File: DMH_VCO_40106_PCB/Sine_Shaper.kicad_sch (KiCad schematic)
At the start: 13 parts, among them Q5 BC548, Q6 BC548, U3 TL074

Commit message: Component placement ongoing
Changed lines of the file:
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@@
+		)
+	)
+	(text_box "Moved R44=1k to Inputs and Outputs sheet"
+		(exclude_from_sim no)
+		(at 179.07 67.31 0)
+		(size 17.78 7.62)
+		(stroke
+			(width 0)
+			(type default)
+		)
+		(fill
+			(type none)
+		)
+		(effects
+			(font
+				(size 1.27 1.27)
+			)
+			(justify left)
 		)
 	)

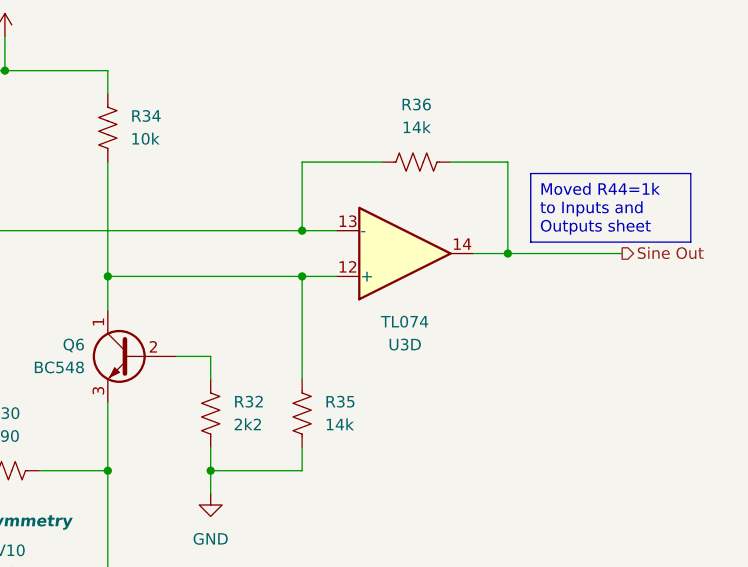
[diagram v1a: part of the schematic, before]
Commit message: Organized Square and Sine Shaper components
Also re-annotated the TL074 ICs to improve the layout
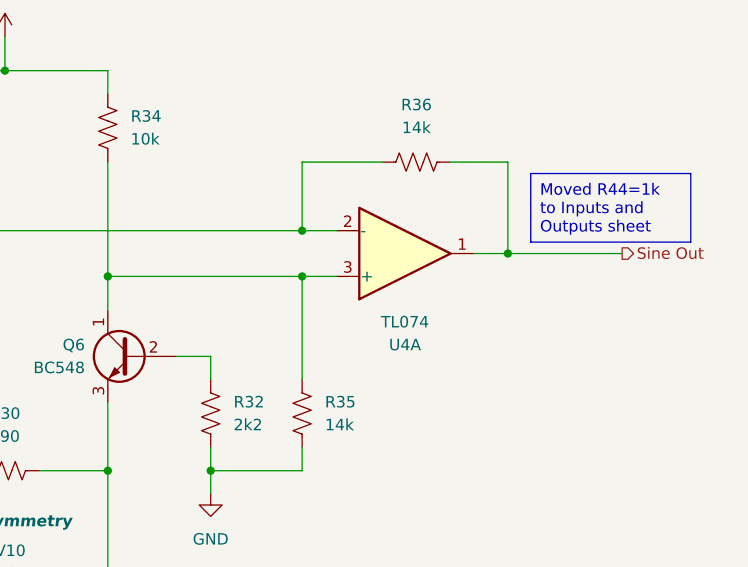
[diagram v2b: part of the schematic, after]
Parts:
- renumbered U3 to U4
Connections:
- net Sine Out: now also U4.1; no longer U4.14
- net at Q5.1 (C), R33.2, R36.1: now also U4.2 (-); no longer U4.13 (-)
- net at Q6.1 (C), R34.2, R35.1: now also U4.3 (+); no longer U4.12 (+)
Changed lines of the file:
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@@
 		(at 165.1 76.2 0)
 		(mirror x)
-		(unit 4)
+		(unit 1)
 		(exclude_from_sim no)
 		(in_bom yes)
 		(on_board yes)
 		(dnp no)
-		(property "Reference" "U3"
+		(property "Reference" "U4"
 			(at 165.1 86.36 0)
 			(effects
@@
 			)
 		)
+		(property "Function" ""
+			(at 165.1 76.2 0)
+			(effects
+				(font
+					(size 1.27 1.27)
+				)
+				(hide yes)
+			)
+		)
 		(pin "9"
 		)
@@
 			(project ""
 				(path "/fefed352-c100-4617-bbfb-c55e7427b122/5d4fa276-24f5-484f-b50d-2ebe5f0666ef"
-					(reference "U3")
-					(unit 4)
+					(reference "U4")
+					(unit 1)
 				)
 			)

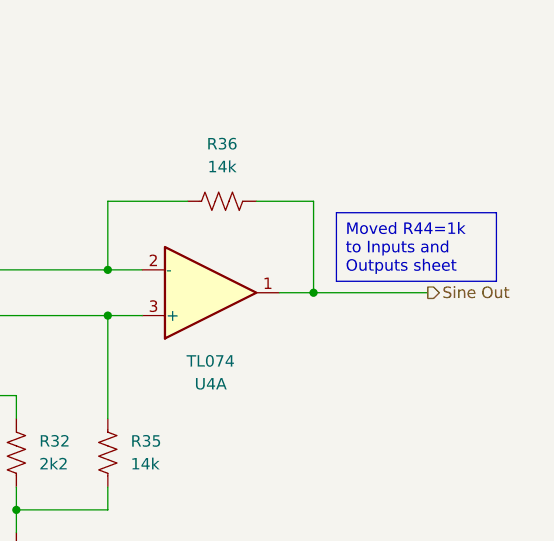
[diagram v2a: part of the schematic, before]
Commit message: Placed input and output resistors back in main PCB
This ensures a more clear schematic and leaves the Connectors PCB only with actual connectors.
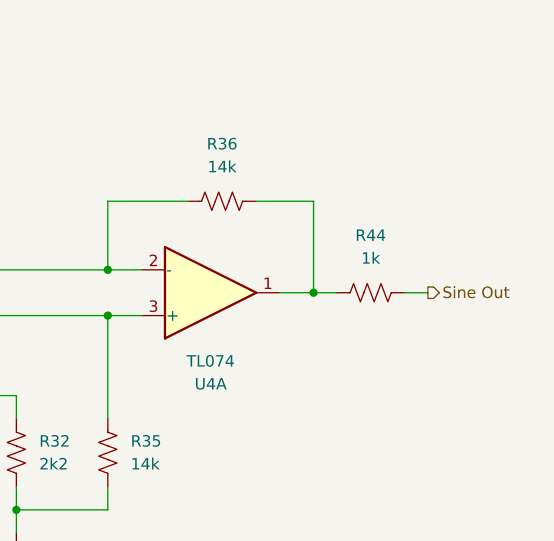
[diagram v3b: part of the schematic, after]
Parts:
- added R44: 1k, Resistor_THT:R_Axial_DIN0207_L6.3mm_D2.5mm_P7.62mm_Horizontal, symbol Device:R_US
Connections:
- net Sine Out: now also R44.1; no longer R36.2, U4.1
- new net: R36.2, R44.2, U4.1
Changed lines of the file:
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@@
 	(wire
 		(pts
-			(xy 176.53 76.2) (xy 189.23 76.2)
+			(xy 176.53 76.2) (xy 179.07 76.2)
 		)
 		(stroke
@@
 	(wire
 		(pts
+			(xy 186.69 76.2) (xy 189.23 76.2)
+		)
+		(stroke
+			(width 0)
+			(type default)
+		)
+	)
+	(wire
+		(pts
 			(xy 132.08 58.42) (xy 132.08 55.88)
 		)
@@
 			(width 0)
 			(type default)
-		)
-	)
-	(text_box "Moved R44=1k to Inputs and Outputs sheet"
-		(exclude_from_sim no)
-		(at 179.07 67.31 0)
-		(size 17.78 7.62)
-		(stroke
-			(width 0)
-			(type default)
-		)
-		(fill
-			(type none)
-		)
-		(effects
-			(font
-				(size 1.27 1.27)
-			)
-			(justify left)
 		)
 	)
@@
 					(unit 1)
 				)
+			)
+		)
+	)
+	(symbol
+		(lib_id "Device:R_US")
+		(at 182.88 76.2 270)
+		(unit 1)
+		(exclude_from_sim no)
+		(in_bom yes)
+		(on_board yes)
+		(dnp no)
+		(fields_autoplaced yes)
+		(property "Reference" "R44"
+			(at 182.88 69.85 90)
+			(effects
+				(font
+					(size 1.27 1.27)
+				)
+			)
+		)
+		(property "Value" "1k"
+			(at 182.88 72.39 90)
+			(effects
+				(font
+					(size 1.27 1.27)
+				)
+			)
+		)
+		(property "Footprint" "Resistor_THT:R_Axial_DIN0207_L6.3mm_D2.5mm_P7.62mm_Horizontal"
+			(at 182.626 77.216 90)
+			(effects
+				(font
+					(size 1.27 1.27)
+				)
+				(hide yes)
+			)
+		)
+		(property "Datasheet" "~"
+			(at 182.88 76.2 0)
+			(effects
+				(font
+					(size 1.27 1.27)
+				)
+				(hide yes)
+			)
+		)
+		(property "Description" "Resistor, US symbol"
+			(at 182.88 76.2 0)
+			(effects
+				(font
+					(size 1.27 1.27)
+				)
+				(hide yes)
+			)
+		)
+		(pin "2"
+		)
+		(pin "1"
+		)
+		(instances
+			(project "DMH_VCO_40106_PCB"
+				(path "/fefed352-c100-4617-bbfb-c55e7427b122/5d4fa276-24f5-484f-b50d-2ebe5f0666ef"
+					(reference "R44")
+					(unit 1)
+				)

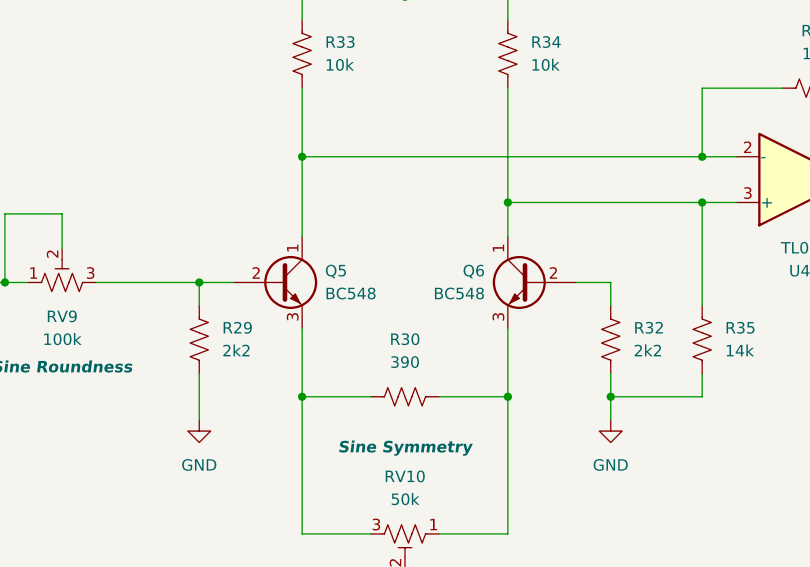
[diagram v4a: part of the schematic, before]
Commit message: Changed buffer resistor to 10M
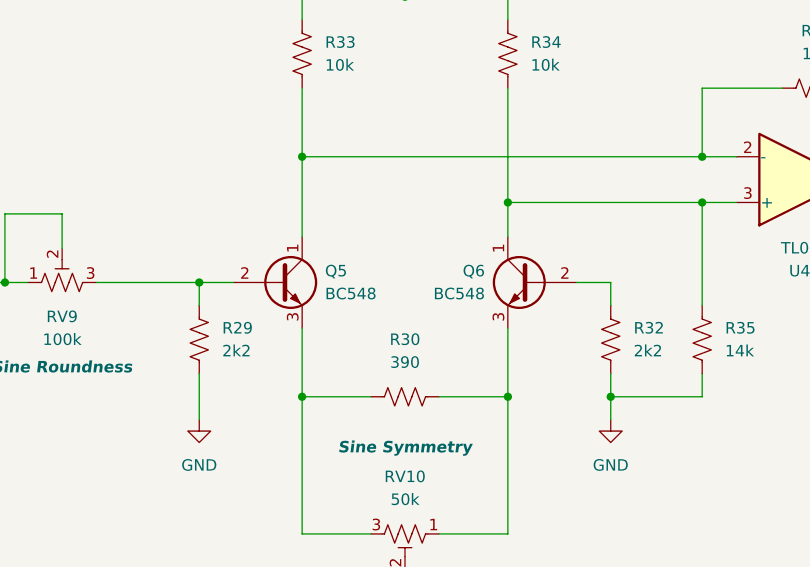
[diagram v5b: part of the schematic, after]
